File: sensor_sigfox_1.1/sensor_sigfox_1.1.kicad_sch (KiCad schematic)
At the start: 18 parts, among them IC1 WSSFM11R2DAT, J1 Battery, J2 Conn_01x07_Socket, J3 Conn_01x01_Female, J4 Antenna, U1 ATtiny826-X, U2 MLX90393, Y1 32.768 kHz

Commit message: gerber y conexiones int/trig
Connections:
- net at U1.2 (PA3): now also U2.1 (INT)
- net at U1.5 (PA4): now also U2.7 (INT/TRIG)

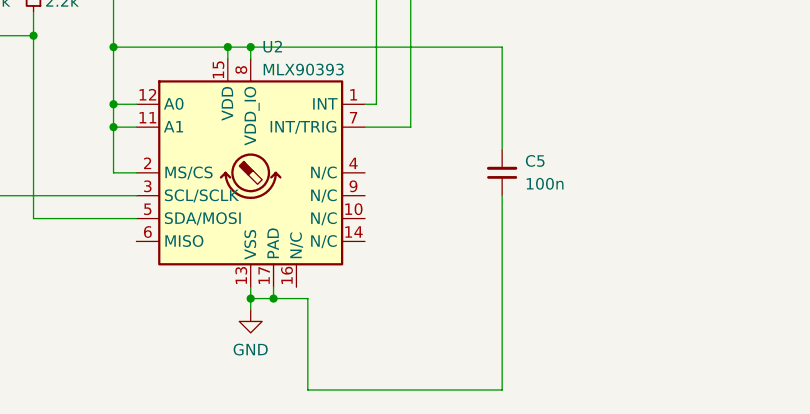
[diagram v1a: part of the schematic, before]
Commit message: 1.1 y 1.2 actualizados
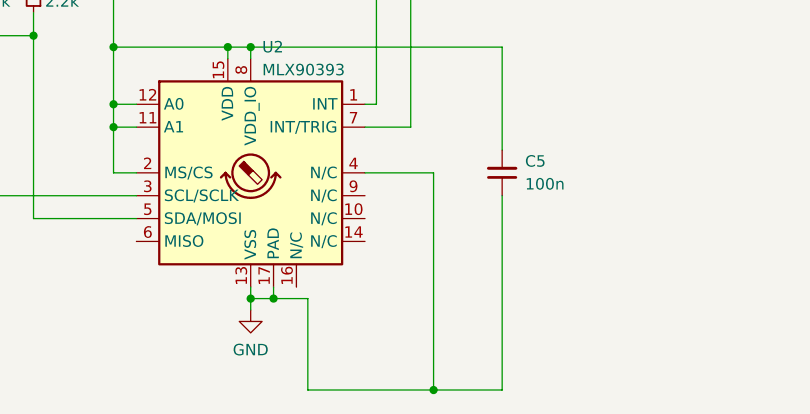
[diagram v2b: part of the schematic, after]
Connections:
- net GND: now also U2.4 (N/C)
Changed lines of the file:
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@@
+	)
+	(junction
+		(at 170.18 143.51)
+		(diameter 0)
+		(color 0 0 0 0)
 	)
 	(junction
@@
 	(wire
 		(pts
-			(xy 177.8 143.51) (xy 156.21 143.51)
+			(xy 177.8 143.51) (xy 170.18 143.51)
 		)
 		(stroke
@@
 	(wire
 		(pts
+			(xy 162.56 119.38) (xy 170.18 119.38)
+		)
+		(stroke
+			(width 0)
+			(type default)
+		)
+	)
+	(wire
+		(pts
 			(xy 142.24 78.74) (xy 142.24 45.72)
 		)
@@
 	(wire
 		(pts
+			(xy 170.18 119.38) (xy 170.18 143.51)
+		)
+		(stroke
+			(width 0)
+			(type default)
+		)
+	)
+	(wire
+		(pts
 			(xy 58.42 63.5) (xy 58.42 66.04)
 		)
@@
 		)
 		(stroke
+			(width 0)
+			(type default)
+		)
+	)
+	(wire
+		(pts
+			(xy 170.18 143.51) (xy 156.21 143.51)
+		)
+		(stroke
